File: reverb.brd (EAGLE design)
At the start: 152.4 x 25.4 mm, 59 parts, among them IC2 TL074, IC2_EQ1 NE5532, IC4_DRV_RCVR TL072, T1 2N3904

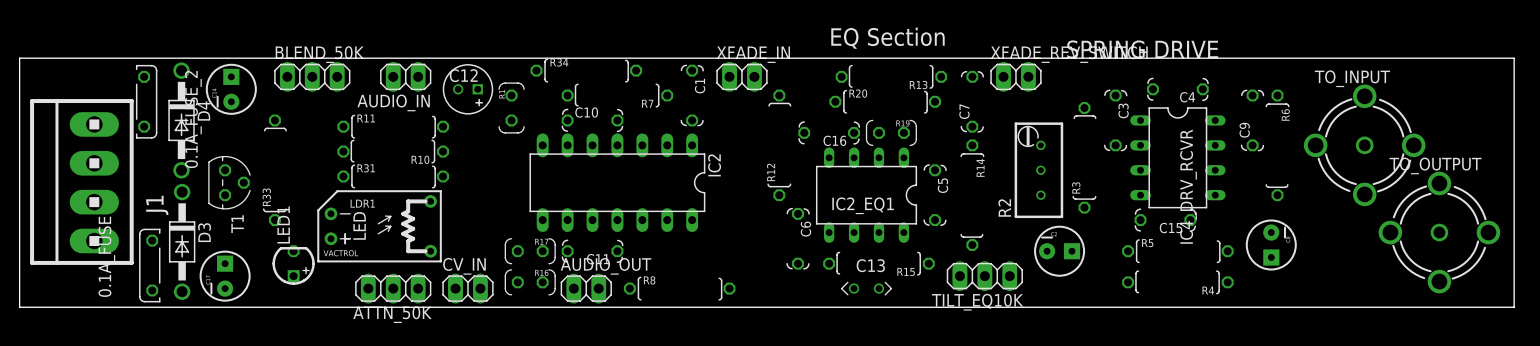
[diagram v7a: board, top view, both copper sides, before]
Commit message: oops, grounds weren't connected..
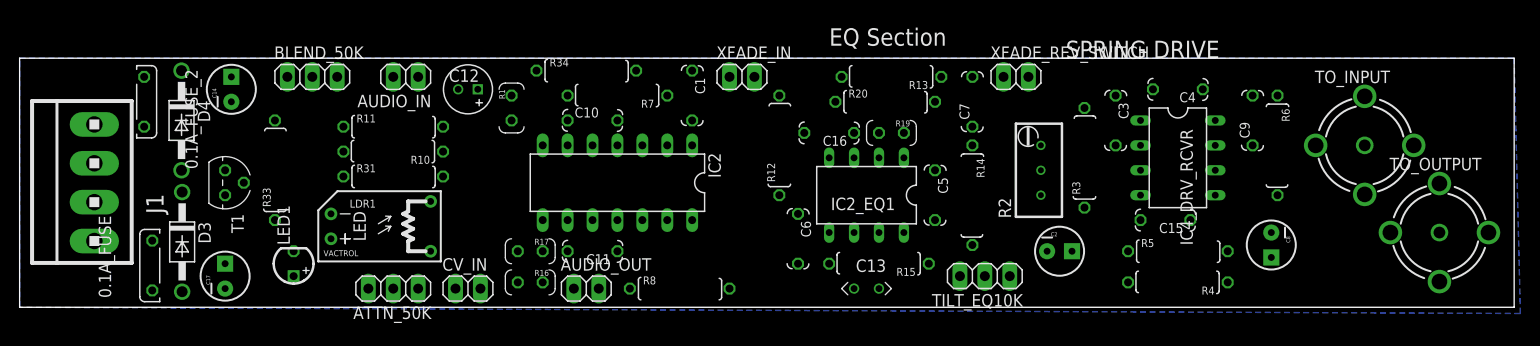
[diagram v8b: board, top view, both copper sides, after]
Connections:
- removed net GND_B: C14.2, C15.1, C17.1, C4.2, D3.C, D4.A, J1.2, J1.3, R2.2, R2.3, R4.2, R5.1, TO_OUTPUT.S
- net GND: now also C14.2, C15.1, C17.1, C4.2, D3.C, D4.A, J1.2, J1.3, R2.2, R2.3, R4.2, R5.1, TO_OUTPUT.S
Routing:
- added copper zone on layer 16, net GND
